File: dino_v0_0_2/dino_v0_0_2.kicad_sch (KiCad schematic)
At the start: 18 parts, among them SW2 RESET_BTN, U20 74LS163, U27 74LS74, U56 74HC14, U6 74LS163, U61 74LS02, U7 74LS138, U8 74LS138, Y1 4MHz

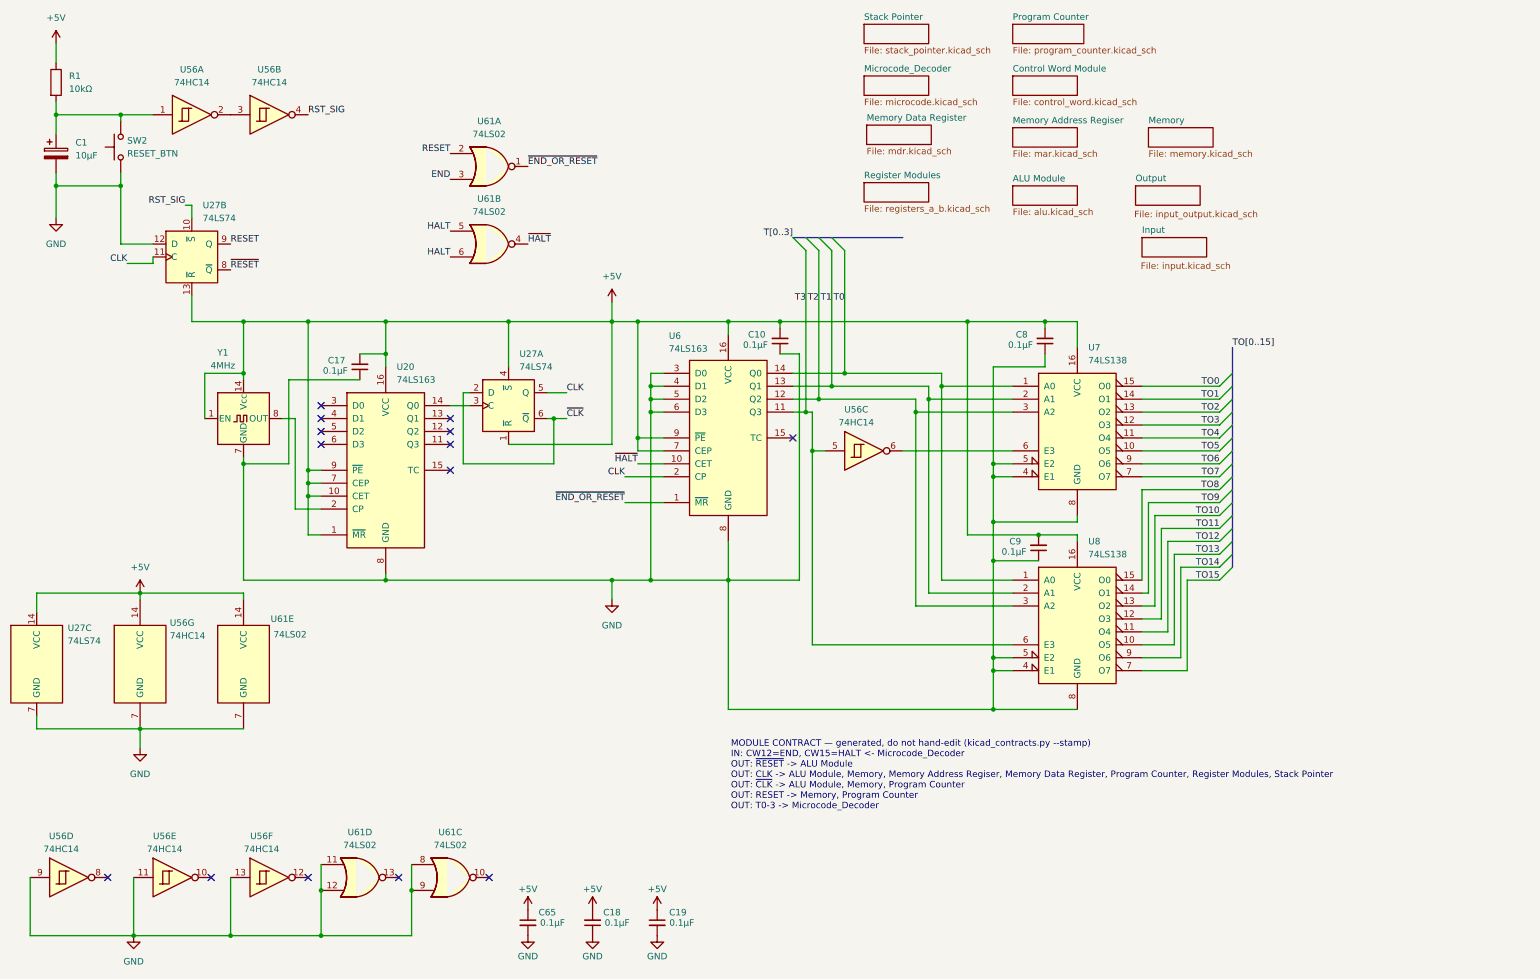
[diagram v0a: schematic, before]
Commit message: feat: Phase F/F+ ISA: 174 instructions, timing fixes, and robust tooling
This commit integrates Phase F and F+ of the ISA, expanding the instruction set to 174 instructions. This includes:
- New conditional branch `JNC`, register-to-register moves, SP/PC readbacks and manipulation (HLSP/SPHL, INXSP/DCXSP).
- Indexed memory access (LDAX/STAX), SP-relative memory access (LDAS/STAS), and memory-indirect addressing (LDAM/STAM/JMPM, etc.) as a new addressing mode.
- Immediate ALU operations (ADI, SUI, ANI, etc.) and ALU results directly to B/C or memory.
- Compare-only instructions (CMP, TST).
- The `IN` opcode has been fully retired from the ISA as of 2026-08-27, and `0x00` confirmed as `NOP`.

Crucially, this commit resolves several critical hardware stability issues:
- Eliminated random machine halts by replacing a damaged `74HC14` (`U56`) and rewiring the reset chain.
- Fixed intermittent failures in `PROG_isasoak` due to ground bounce by starring GND/VCC connections (2026-09-01).
- Introduced microcode-level "SETTLE" states for 23 ALU instructions to ensure timing margins at 1.024MHz, resolving timing-dependent failures for instructions that load and consume operands in consecutive T-states.

The development tooling has also been significantly improved for robustness and accuracy:
- The assembler (`asm.py`) now uses `microcode_gen.py` as the single source of truth for ISA definitions.
- New self-checking ISA tests (`PROG_isa` and variants) were developed, incorporating mutation testing to verify subtest efficacy and provide detailed diagnostic feedback for debugging marginality or hangs.
- The microcode generator enforces hardware constraints at build time (e.g., valid `cond` flag selections, preventing `src=ROM` `dst=RAM` conflicts that led to the `MVI` bug).
- The simulator (`progrom_gen.py`) accurately models `OUT` latching the bus and `dst=RAM` writing to the address bus, and refuses to guess undefined `FLAG_C` states after logic operations.
- The root `Makefile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
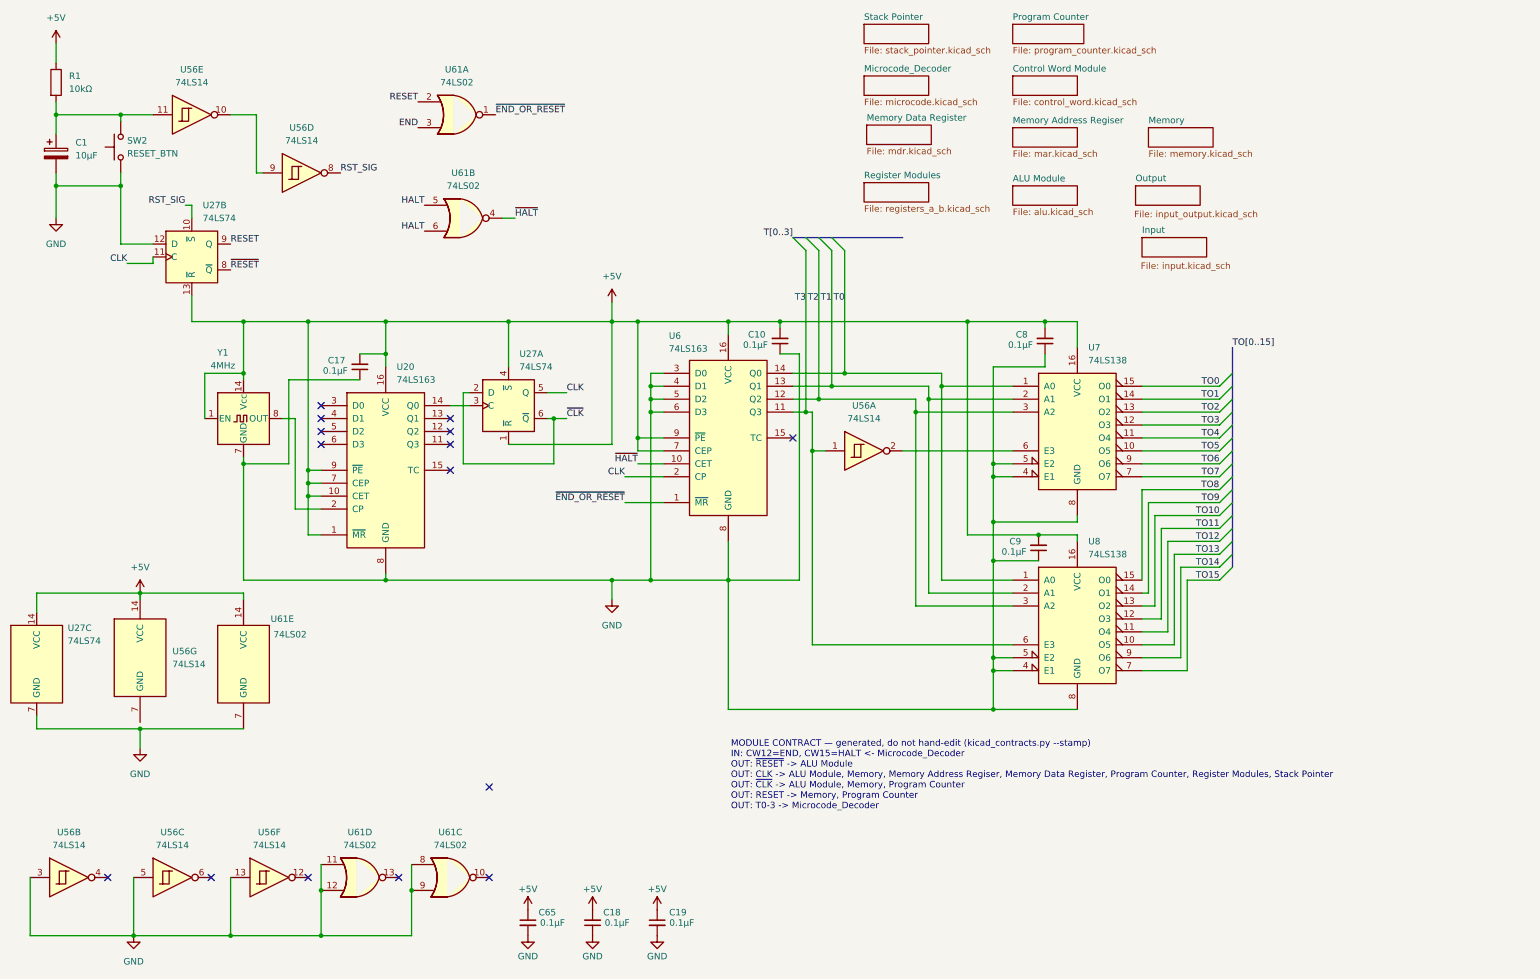
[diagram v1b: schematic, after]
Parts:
- removed U56: 74HC14, symbol 74xx:74HC14
- added U56: 74LS14, symbol 74xx:74LS14
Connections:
- net +5V: now also U56.14 (VCC)
- net GND: now also U56.13, U56.3, U56.5
- net RST_SIG: now also U56.8
- net T3: now also U56.1
- net at U7.6 (E3): now also U56.2
- net at C1.1, R1.2, SW2.2: now also U56.11
- new net: U56.10, U56.9
- no-connect marks 14 -> 15
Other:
- moved on the sheet: U61A, U61B

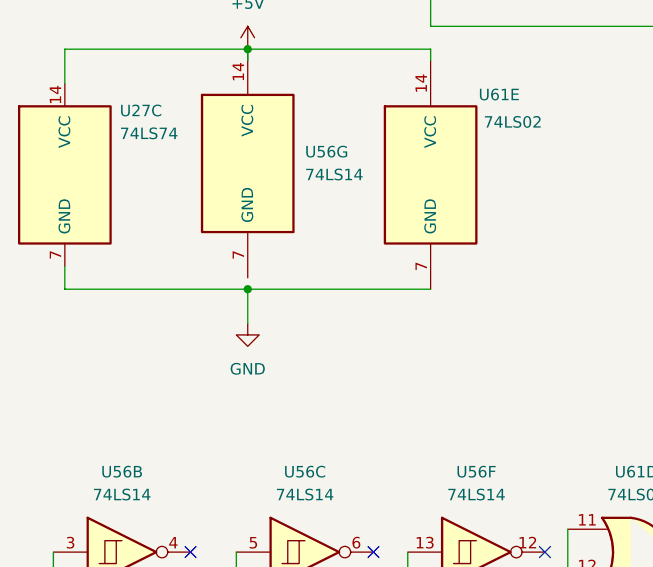
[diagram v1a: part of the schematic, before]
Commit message: feat: phase G on silicon -- serial card, 9600 8N1, echo proven
The PC16550D card (U101 '138, U102 '245, U103, dino_serial/) runs on the
bench. Every step-4..8 witness passed 2026-09-04: serid 0x55, serid_aa
0xAA, serlsr 0x60, seriir 0xC1, serbaud 153.6 kHz on U103.15, serloop
0x53, sertx "DINO" on the host terminal, serrx echoing a typed character
on OB and back to the host. The data bus is PROVEN, not narrowed: a
receiver DINO does not control decoded it.

Two bench faults found and fixed on the way, both copper, neither
visible to --continuity:
  - the card's ~WR was on U75.5 (an input) instead of U75.6; ~{IO_WR}
    now feeds a real consumer for the first time.
  - C1 was 1uF in the socket against 10uF in the drawing, so the machine
    had no power-on reset: reset released ~1ms into the rail ramp and the
    UART started un-reset, framing 5-bit characters until the button
    gave it its first real MR. 10uF fitted; cold boot is clean. New rule
    in CLAUDE.md: a component value is copper too.

Tooling:
  - progrom_gen.Unoracled: the oracle's by-design refusals (non-SCR UART
    registers, undefined carry) are a subclass; asm.py --run reports them
    and still writes the image instead of dying in make burn-prog-*.
    roms_readme_gen lists such images as UNORACLED.
  - docs/notes/serprobe_host.py: stdlib host probe, sends bytes and prints
    every returned byte in hex with timing. Replaces the terminal as the
    serial witness.
  - docs/notes/test_serial_card.py: the card schematic's paper witness.
  - Makefile: make monitor / kill-monitor.

Images: the eight phase G witnesses, five diagnostics from the cold-boot
chase (serrx0, serlcr, serlive, serrxlcr, serrxlive), and the phase F
coverage ROMs that were on disk but never committed.

Co-Authored-By: Claude Fable 5.1 <noreply@anthropic.com>
Claude-Session: https://claude.ai/code/session_01WMy1UioY1p8BufsC2zZ3hR
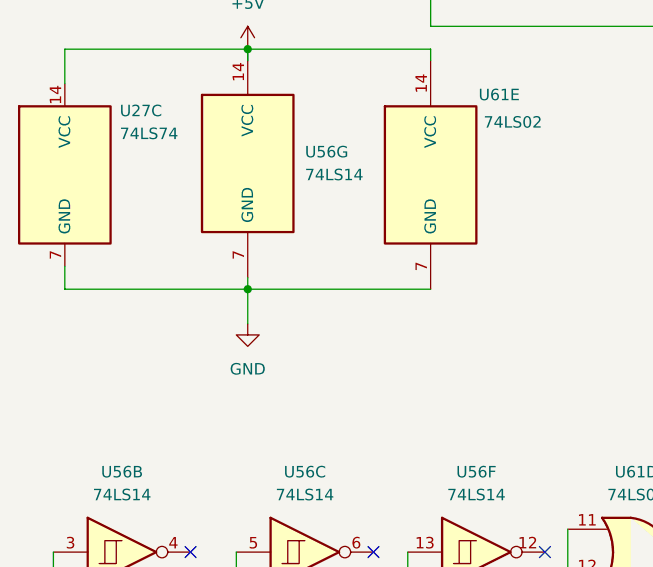
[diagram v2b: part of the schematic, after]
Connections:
- net GND: now also U56.7 (GND)
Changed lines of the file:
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@@
+	(wire
+		(pts
+			(xy 40.64 153.67) (xy 40.64 154.94)
+		)
+		(stroke
+			(width 0)
+			(type default)
+		)
+	)
 	(wire
 		(pts

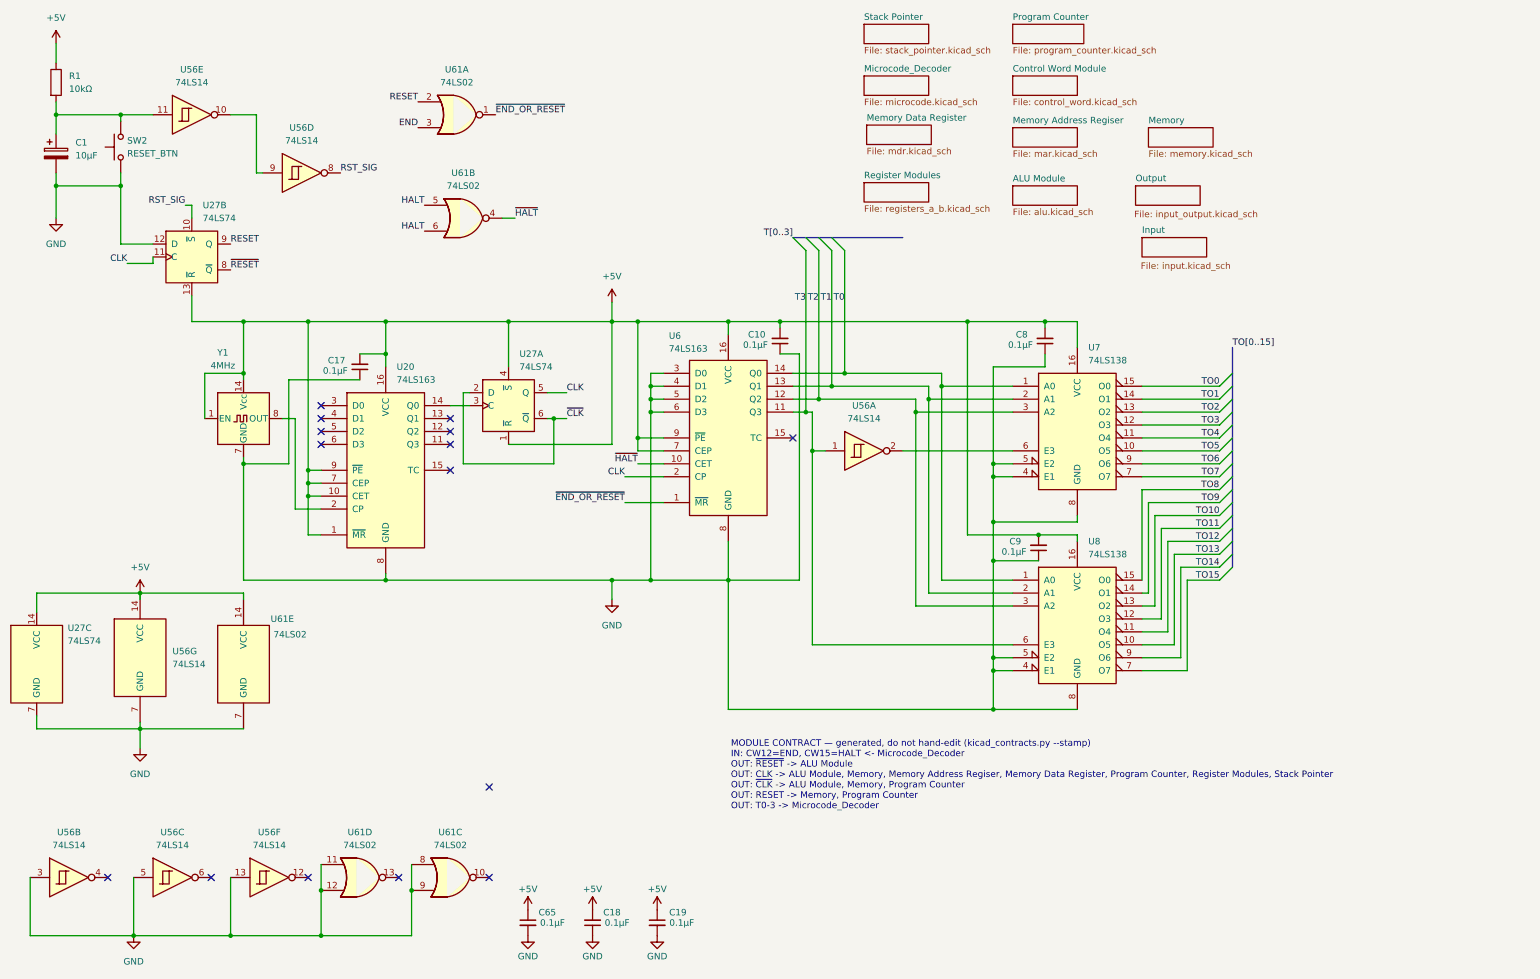
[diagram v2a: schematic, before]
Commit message: feat(kicad): footprints, power sheet, global labels, PCB draft
Every symbol gets a stock THT footprint (plain DIP, no sockets, so the
3D render shows ICs). New Power sheet: 24-pin ATX header for a picoPSU,
rails +5V/+3.3V/+12V/-12V/GND only; no -5V exists on any ATX unit since
2003, none drawn. PS_ON# on a 2-pin header.

Cross-sheet labels become global labels. KiCad joined nothing between
sheets before: 122 base names were split per sheet, ERC saw 90 undriven
inputs whose driver sat one sheet away, and the PCB ratsnest stopped at
every sheet boundary. Proof: KiCad's netlist after equals a name-join of
its netlist before plus the 15 CW alias pairs, pin for pin.

kicad_contracts took a node's sheet from the net name's /Sheet/ prefix;
global nets have none, so it emitted an empty contracts doc. Sheet now
comes from the component's own path; the doc regenerates with zero diff.

ERC 477 -> 2. Real fixes: ROM I/O pins input -> tri_state, '382 GND pin
power_out -> power_in, four orphan symbols rehomed to project lib `dino`,
one stub wire. 133 by-design warnings excluded by uuid ('245 readback on
counter Q, alias stubs, probe-point labels); the two left are bus
signals the peripheral bus sheet will consume.

PCB draft: 198 footprints placed per sheet, all pads netted, no tracks.

Co-Authored-By: Claude Fable 5.1 <noreply@anthropic.com>
Claude-Session: https://claude.ai/code/session_018irreFHb1xEykW5kCD26ow
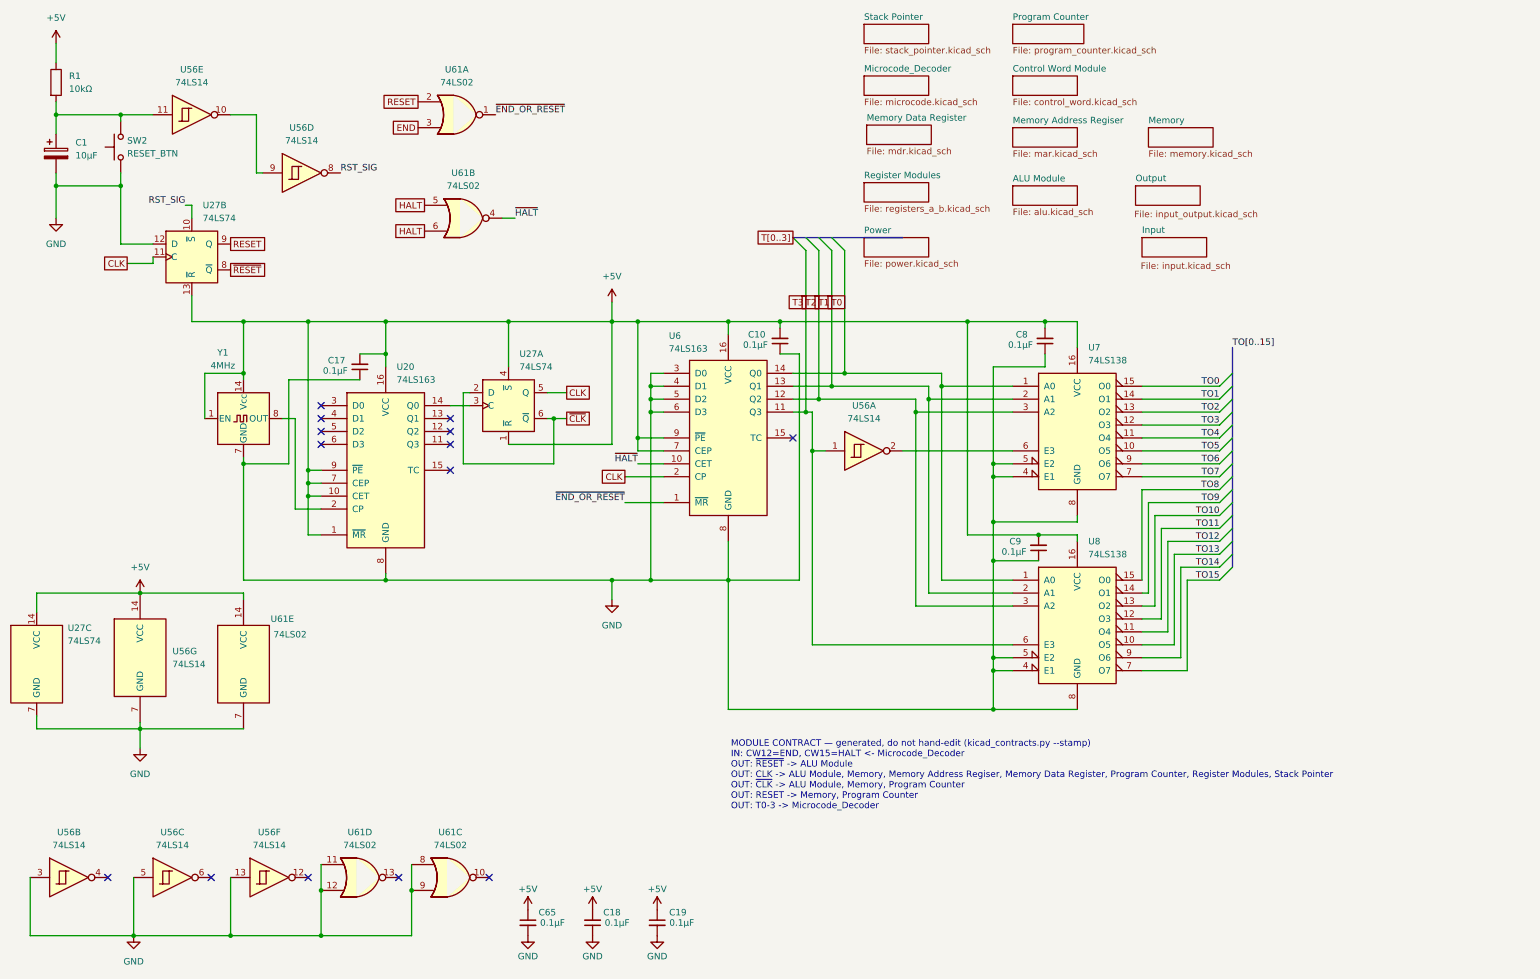
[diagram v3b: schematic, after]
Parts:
- C1: footprint (none) -> Capacitor_THT:CP_Radial_D5.0mm_P2.00mm
- C10, C17, C18, C19, C65, C8, C9: footprint (none) -> Capacitor_THT:C_Disc_D5.0mm_W2.5mm_P2.50mm
- R1: footprint (none) -> Resistor_THT:R_Axial_DIN0207_L6.3mm_D2.5mm_P10.16mm_Horizontal
- SW2: footprint (none) -> Button_Switch_THT:SW_PUSH_6mm
- U20, U6, U7, U8: footprint (none) -> Package_DIP:DIP-16_W7.62mm
- U27, U56, U61: footprint (none) -> Package_DIP:DIP-14_W7.62mm
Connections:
- no-connect marks 15 -> 14
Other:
- added sheet Power (power.kicad_sch)
